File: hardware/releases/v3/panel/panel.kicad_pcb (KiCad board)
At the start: 4 copper layers, 55.6 x 78 mm, 101 parts, among them J1 KNX bus terminal pins, J101 Carrier, J102 OLED ZIF, J2 AUX 20-32 V (yellow/white), J3 DALI bus (push-in), J4 UI board, Q1 MJD45H11, Q2 BC857, Q3 IRLML0060, Q4 BC847, Q5 BC847, Q6 BC847, SW101 PRG/RST, SW102 FUNC, U1 NCN5130MNTWG, U101 74AHCT1G125, U2 SCT2400TVBR, U3 REM3-2415S/A/CTRL 24V->15V 3W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, U4 TLP383, U5 TLP383(D4BLLTL,E, U6 TLP383(D4BLLTL,E, U7 LM66100, U8 XIAO ESP32C6, Y1 16MHz

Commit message: Added custom naming support for channels and groups with persistent storage, D4i power polling during commissioning, and updated web UI to display and edit names in lamp/group tiles and inspector panels
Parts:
- removed MOUSE_BITES: DNP, 
- added MB1: DNP, , F.Cu at (39.9, -31.3)
- added MB10: DNP, , F.Cu at (41.6, -11.0)
- added MB11: DNP, , F.Cu at (39.9, -10.4)
- added MB12: DNP, , F.Cu at (41.6, -10.4)
- added MB13: DNP, , F.Cu at (39.9, -9.82)
- added MB14: DNP, , F.Cu at (41.6, -9.82)
- added MB15: DNP, , F.Cu at (39.9, -9.22)
- added MB16: DNP, , F.Cu at (41.6, -9.22)
- added MB2: DNP, , F.Cu at (41.6, -31.3)
- added MB3: DNP, , F.Cu at (39.9, -30.7)
- added MB4: DNP, , F.Cu at (41.6, -30.7)
- added MB5: DNP, , F.Cu at (39.9, -30.1)
- added MB6: DNP, , F.Cu at (41.6, -30.1)
- added MB7: DNP, , F.Cu at (39.9, -29.5)
- added MB8: DNP, , F.Cu at (41.6, -29.5)
- added MB9: DNP, , F.Cu at (39.9, -11.0)

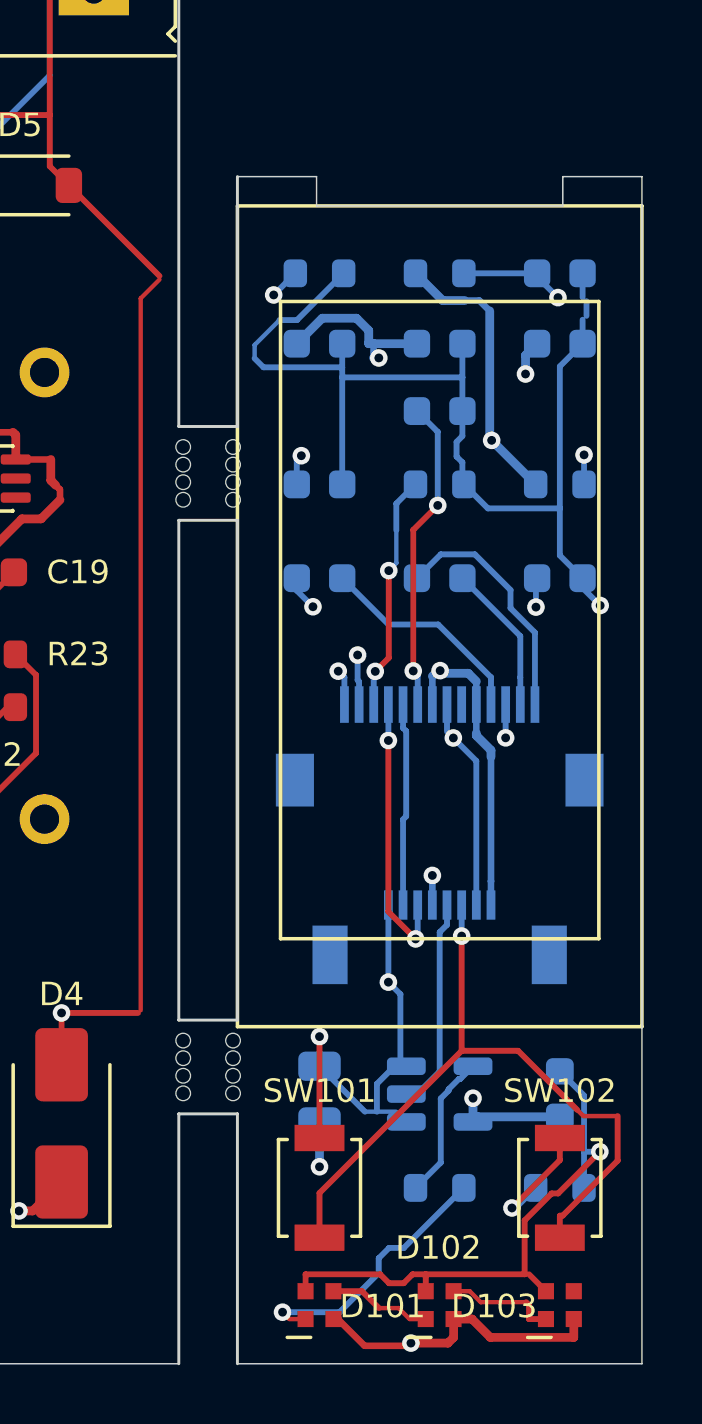
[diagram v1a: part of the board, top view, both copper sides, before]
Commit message: Replaced V3 OLED connector from 14-pin 0.5mm ZIF FPC to 14-pin 0.62mm pitch direct-solder FPC footprint, relocated UI board passives to accommodate new layout with top-edge notch adjusted to 9.8mm width for 12mm flex tail, and updated assembly documentation with NFP1312-15AY part number and pre-applied mounting tape details
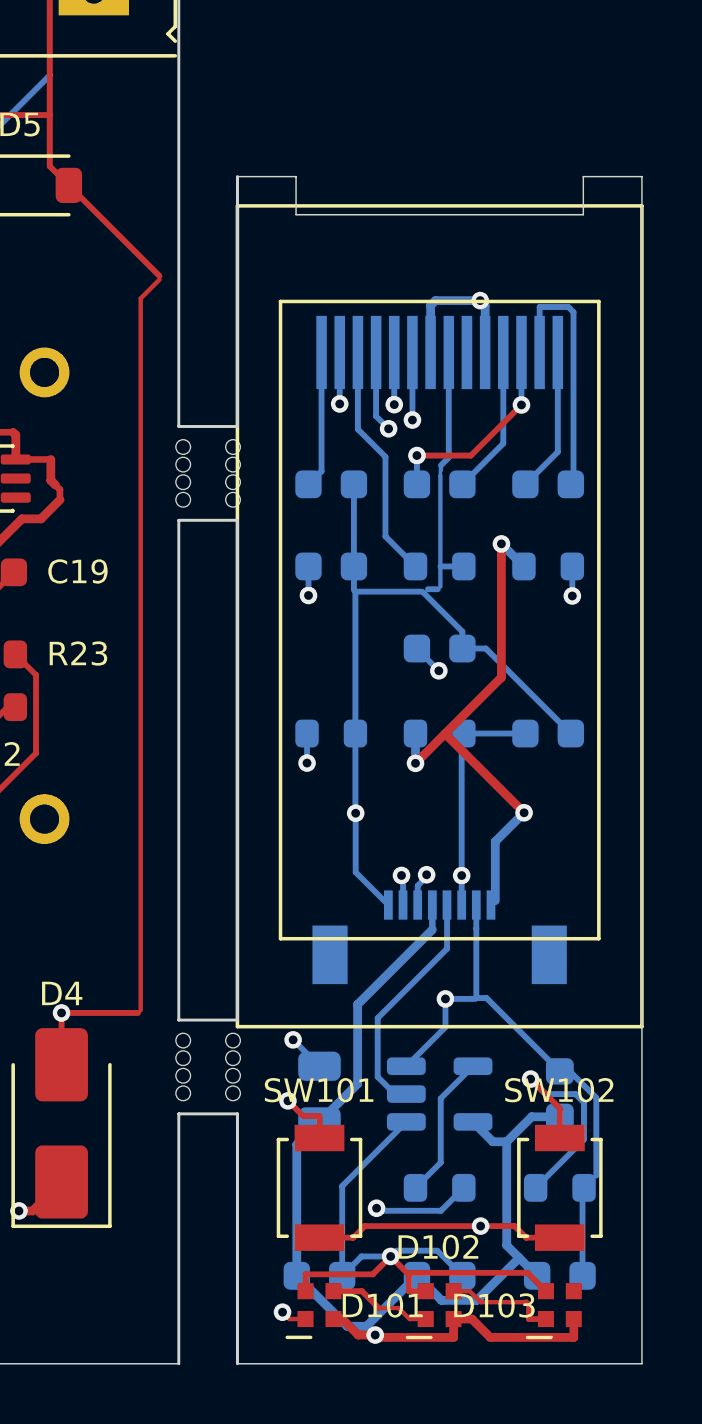
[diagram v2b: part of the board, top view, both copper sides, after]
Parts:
- J102: value OLED ZIF -> OLED; footprint gateway_fp:FPC_XUNPU_FPC-05F-14PH20 -> gateway_fp:OLED_FPC_14P_P0.62mm_Hotbar
- moved C104 31.8 mm to (44.6, -3.00)
- moved C105 31.8 mm to (48.7, -3.00)
- moved C106 31.8 mm to (52.8, -3.00)
- moved C101 15.7 mm to (52.4, -21.5)
- moved R102 15.7 mm to (45.0, -21.5)
- moved R101 15.7 mm to (48.7, -21.5)
- moved J102 13.3 mm to (48.7, -34.5)
- moved C107 8.10 mm to (48.7, -24.4)
- moved C110 7.81 mm to (45.0, -27.2)
- moved C108 5.20 mm to (48.7, -30.0)
- moved C109 4.89 mm to (52.4, -30.0)
- moved R105 2.83 mm to (52.4, -27.2)
- moved R106 2.80 mm to (48.7, -27.2)
- moved C111 0.40 mm to (45.0, -30.0)
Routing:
- net UI_+5V: track 72.7 -> 43.5 mm, vias 6 -> 1
- net UI_BTN_LADDER: track 53.3 -> 28.7 mm
- net UI_I2C_SCL: track 6.93 -> 24.1 mm, vias 0 -> 2
- net UI_N$1: track 31.0 -> 15.2 mm
- net UI_I2C_SDA: track 9.57 -> 19.9 mm
- net UI_OLED_C1P: track 12.6 -> 7.05 mm
- net UI_OLED_VOUT: track 10.1 -> 4.68 mm, vias 2 -> 0
- net UI_N$2: track 4.16 -> 8.17 mm
- net UI_OLED_C2N: track 5.13 -> 8.69 mm
- net UI_OLED_C2P: track 8.28 -> 4.96 mm
- net UI_+3V3: track 29.7 -> 32.1 mm, vias 2 -> 4
- net UI_OLED_C1N: track 7.40 -> 5.08 mm
- net UI_OLED_VCOMH: track 11.0 -> 9.72 mm
- net UI_LED_DATA: track 7.24 -> 8.06 mm
- net UI_N$4: track 9.12 -> 9.10 mm, vias 1 -> 2
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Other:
- outline, holes or cut-outs redrawn
